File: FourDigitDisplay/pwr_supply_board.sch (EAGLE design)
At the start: 0 parts

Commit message: 電源回路図の初版
12Vから170V、5Vの２電源を生成し出力させる回路
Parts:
- added C1: 100uF/16V, Parts:ELECAP_200MIL
- added C2: 1500pF, Parts:CAP_200MIL
- added C3, C4: 33uF/400V, Parts:ELECAP_300MIL
- added C5, C6: 1uF, Parts:CAP_200MIL
- added CN1, CN2, CN3: POWER_IF, PartsForProto:POWER_IF
- added D1: 1S1585, Parts:1S1585
- added D2: ER504, Parts:ER504
- added L1: 220uH, Parts:TC5026-220UH-050
- added L2: 22uH, Parts:TC5026-22UH-060
- added Q1: 2SA1020L-Y, Parts:2SA1020L-Y
- added Q2: 2SK3234, Parts:2SK3234
- added R1: 0.3, Parts:RESISTOR_600MIL
- added R2, R4: 1k, Parts:RESISTOR_600MIL
- added R3: 620, Parts:RESISTOR_600MIL
- added R5: 100k, Parts:RESISTOR_600MIL
- added R6: 750, Parts:RESISTOR_600MIL
- added R7: 10, Parts:RESISTOR_600MIL
- added U1: MC34063AP1, Parts:MC34063AP1
- added U5: XC6202P502TB, Parts:XC6202P502TB
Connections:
- new net +12V: C1.+, C6.1, CN1.VDD, R1.1, U1.VCC, U5.VIN
- new net +24V: C4.+, CN2.VDD, L2.2
- new net +5V: C5.1, CN3.VDD, U5.VOUT
- new net 0V: C1.-, C2.2, C3.-, C4.-, C5.2, C6.2, CN1.GND, CN2.GND, CN3.GND, Q1.C, Q2.S, R4.1, R7.1, U1.GND, U5.VSS
- new net N$1: R3.1, U1.DC
- new net N$10: D2.A, L1.2, Q2.D
- new net N$2: C3.+, D2.C, L2.1, R5.2
- new net N$3: C2.1, U1.TC
- new net N$4: R2.1, U1.SC
- new net N$5: L1.1, R1.2, R2.2, R3.2, U1.ISENSE
- new net N$6: R5.1, R6.2, U1.INVIN
- new net N$7: D1.A, Q1.B, R4.2, U1.SE
- new net N$8: D1.C, Q1.E, Q2.G
- new net N$9: R6.1, R7.2

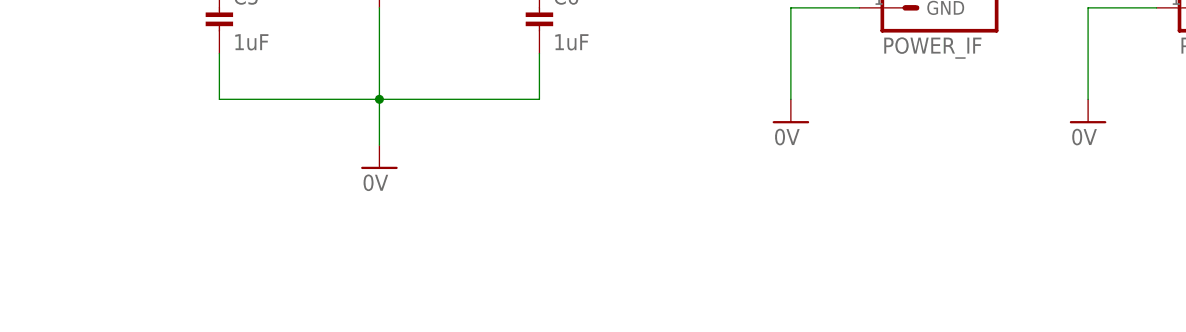
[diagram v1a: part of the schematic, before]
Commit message: マウントホール追加
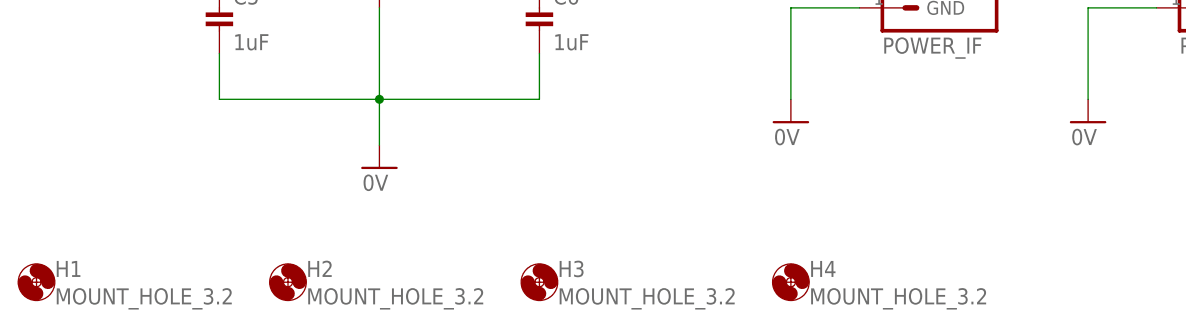
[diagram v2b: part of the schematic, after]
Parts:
- added H1, H2, H3, H4: MOUNT_HOLE_3.2, Generic:MOUNT_HOLE_3.2
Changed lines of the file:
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@@
 <setting verticaltext="up"/>
 </settings>
-<grid distance="25" unitdist="mil" unit="mil" style="dots" multiple="1" display="yes" altdistance="0.01" altunitdist="inch" altunit="inch"/>
+<grid distance="0.1" unitdist="inch" unit="inch" style="lines" multiple="1" display="no" altdistance="0.01" altunitdist="inch" altunit="inch"/>
 <layers>
 <layer number="1" name="Top" color="4" fill="1" visible="no" active="no"/>
@@
 <part name="GND4" library="Supply" deviceset="0V" device=""/>
 <part name="P+8" library="Supply" deviceset="+5V" device=""/>
+<part name="H1" library="Generic" deviceset="MOUNT_HOLE" device="_3.2"/>
+<part name="H2" library="Generic" deviceset="MOUNT_HOLE" device="_3.2"/>
+<part name="H3" library="Generic" deviceset="MOUNT_HOLE" device="_3.2"/>
+<part name="H4" library="Generic" deviceset="MOUNT_HOLE" device="_3.2"/>
 </parts>
 <sheets>
@@
 <attribute name="VALUE" x="179.705" y="62.23" size="1.778" layer="96"/>
 </instance>
+<instance part="H1" gate="G$1" x="33.02" y="15.24"/>
+<instance part="H2" gate="G$1" x="60.96" y="15.24"/>
+<instance part="H3" gate="G$1" x="88.9" y="15.24"/>
+<instance part="H4" gate="G$1" x="116.84" y="15.24"/>
 </instances>
 <busses>

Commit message: 部品配置
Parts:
- C2, C5, C6: device Parts:CAP_200MIL -> Parts:CAP_100MIL
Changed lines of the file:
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@@
 <part name="R3" library="Parts" deviceset="RESISTOR" device="_600MIL" value="620"/>
 <part name="R4" library="Parts" deviceset="RESISTOR" device="_600MIL" value="1k"/>
-<part name="C2" library="Parts" deviceset="CAP" device="_200MIL" value="1500pF"/>
+<part name="C2" library="Parts" deviceset="CAP" device="_100MIL" value="1500pF"/>
 <part name="U1" library="Parts" deviceset="MC34063A*" device="P1"/>
 <part name="D1" library="Parts" deviceset="1S1585" device=""/>
@@
 <part name="P+2" library="Supply" deviceset="+170V" device=""/>
 <part name="U5" library="Parts" deviceset="XC6202*" device="P502TB"/>
-<part name="C5" library="Parts" deviceset="CAP" device="_200MIL" value="1uF"/>
-<part name="C6" library="Parts" deviceset="CAP" device="_200MIL" value="1uF"/>
+<part name="C5" library="Parts" deviceset="CAP" device="_100MIL" value="1uF"/>
+<part name="C6" library="Parts" deviceset="CAP" device="_100MIL" value="1uF"/>
 <part name="P+6" library="Supply" deviceset="+12V" device=""/>
 <part name="P+7" library="Supply" deviceset="+5V" device=""/>

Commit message: 電源基板の部品配線
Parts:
- C1: device Parts:ELECAP_200MIL -> Parts:ELECAP_100MIL
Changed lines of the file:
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@@
 <part name="P+1" library="Supply" deviceset="+12V" device=""/>
 <part name="GND1" library="Supply" deviceset="0V" device=""/>
-<part name="C1" library="Parts" deviceset="ELECAP" device="_200MIL" value="100uF/16V"/>
+<part name="C1" library="Parts" deviceset="ELECAP" device="_100MIL" value="100uF/16V"/>
 <part name="R1" library="Parts" deviceset="RESISTOR" device="_600MIL" value="0.3"/>
 <part name="R2" library="Parts" deviceset="RESISTOR" device="_600MIL" value="1k"/>
